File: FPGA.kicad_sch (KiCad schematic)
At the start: 69 parts, among them U1 LCMXO2-7000HC-6TG144I, U11 T602-025.0M

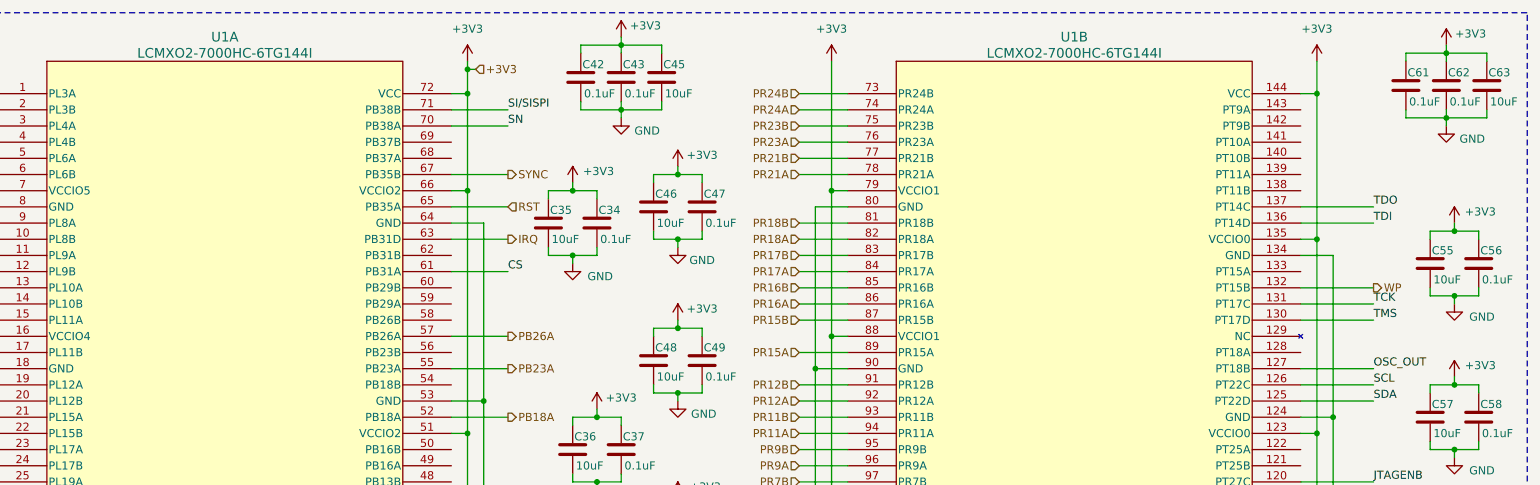
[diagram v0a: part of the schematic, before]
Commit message: Updated libraries
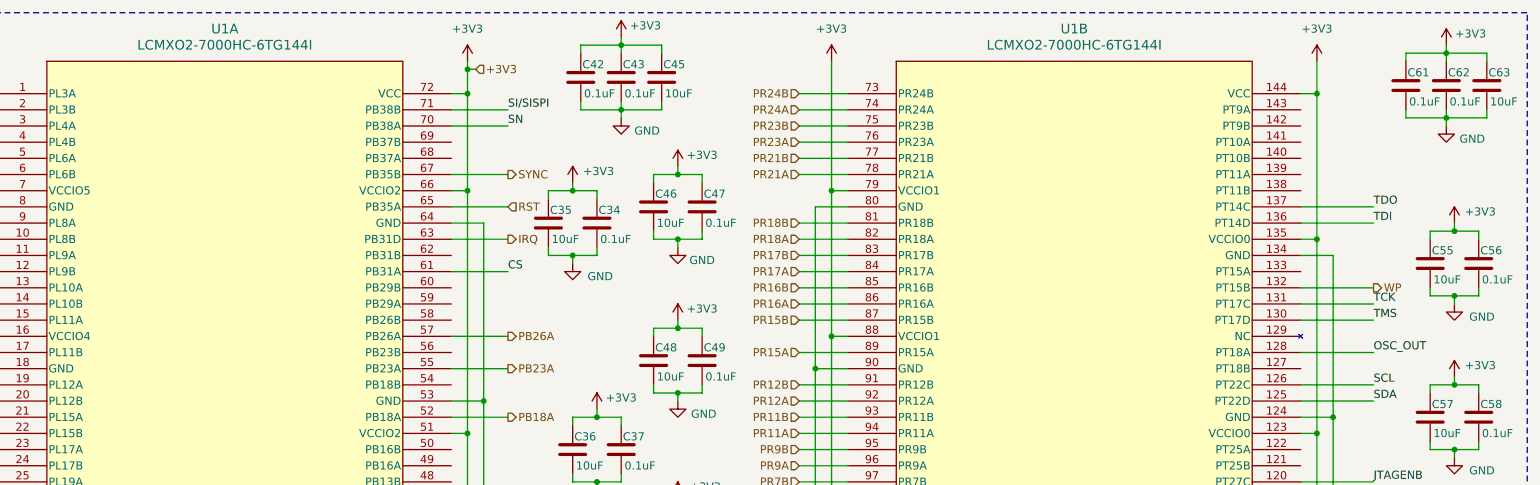
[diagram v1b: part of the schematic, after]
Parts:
- U1: footprint Package_QFP:TQFP144_LAT -> Footprints:TQFP144_LAT; symbol FPGA_Lattice:LCMXO2-7000HC-6TG144I -> Symbols:LCMXO2-7000HC-6TG144I
- U11: footprint Oscillator:T602-025.0M_CNW -> Footprints:T602-025.0M_CNW; symbol Oscillator:T602-025.0M -> Symbols:T602-025.0M
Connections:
- net OSC_OUT: now also U1.128 (PT18A); no longer U1.127 (PT18B)
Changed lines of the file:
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@@
 	(wire
 		(pts
+			(xy 247.65 67.31) (xy 259.08 67.31)
+		)
+		(stroke
+			(width 0)
+			(type default)
+		)
+	)
+	(wire
+		(pts
 			(xy 149.86 90.17) (xy 149.86 91.44)
 		)
@@
 	(wire
 		(pts
-			(xy 247.65 69.85) (xy 259.08 69.85)
-		)
-		(stroke
-			(width 0)
-			(type default)
-		)
-	)
-	(wire
-		(pts
 			(xy 270.51 29.21) (xy 270.51 30.48)
 		)
@@
 		)
 	)
+	(label "OSC_OUT"
+		(at 259.08 67.31 0)
+		(effects
+			(font
+				(size 1.27 1.27)
+			)
+			(justify left bottom)
+		)
+	)
 	(label "SN"
 		(at 78.74 180.34 180)
@@
 		)
 	)
-	(label "OSC_OUT"
-		(at 259.08 69.85 0)
-		(effects
-			(font
-				(size 1.27 1.27)
-			)
-			(justify left bottom)
-		)
-	)
 	(label "JTAGENB"
 		(at 259.08 87.63 0)
@@
 	)
 	(symbol
-		(lib_id "Oscillator:T602-025.0M")
+		(lib_id "Symbols:T602-025.0M")
 		(at 167.64 139.7 0)
 		(unit 1)
@@
 			)
 		)
-		(property "Footprint" "Oscillator:T602-025.0M_CNW"
+		(property "Footprint" "Footprints:T602-025.0M_CNW"
 			(at 167.64 139.7 0)
 			(effects
@@
 	)
 	(symbol
-		(lib_id "FPGA_Lattice:LCMXO2-7000HC-6TG144I")
+		(lib_id "Symbols:LCMXO2-7000HC-6TG144I")
 		(at 176.53 26.67 0)
 		(unit 2)
@@
 		(fields_autoplaced yes)
 		(property "Reference" "U1"
-			(at 212.09 17.78 0)
+			(at 212.09 16.51 0)
 			(effects
 				(font
@@
 		)
 		(property "Value" "LCMXO2-7000HC-6TG144I"
-			(at 212.09 20.32 0)
+			(at 212.09 19.05 0)
 			(effects
 				(font
@@
 			)
 		)
-		(property "Footprint" "Package_QFP:TQFP144_LAT"
+		(property "Footprint" "Footprints:TQFP144_LAT"
 			(at 176.53 26.67 0)
 			(effects
@@
 	)
 	(symbol
-		(lib_id "FPGA_Lattice:LCMXO2-7000HC-6TG144I")
+		(lib_id "Symbols:LCMXO2-7000HC-6TG144I")
 		(at 43.18 26.67 0)
 		(unit 1)
@@
 		(fields_autoplaced yes)
 		(property "Reference" "U1"
-			(at 78.74 17.78 0)
+			(at 78.74 16.51 0)
 			(effects
 				(font
@@
 		)
 		(property "Value" "LCMXO2-7000HC-6TG144I"
-			(at 78.74 20.32 0)
+			(at 78.74 19.05 0)
 			(effects
 				(font
@@
 			)
 		)
-		(property "Footprint" "Package_QFP:TQFP144_LAT"
+		(property "Footprint" "Footprints:TQFP144_LAT"
 			(at 43.18 26.67 0)
 			(effects
